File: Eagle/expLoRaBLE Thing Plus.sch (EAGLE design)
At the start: 65 parts, among them J2 CORTEX_DEBUG, J5 USB-C, J8 U.FL, U1 MCP73831, U2 3.3V, U3 NM180100, U4 CH340E_MSOP10, U6 DPX202700DT-4162A1, Y1 32.768kHz

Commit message: Create prelim board fabrication files
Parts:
- removed R10, R9: 10k, SparkFun-Resistors:10KOHM-0603-1/10W-1%
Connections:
- removed net LORA_EN: U3.GPIO7
- net 3.3V: no longer R10.2, R9.2
- net D14/QWIIC_SDA: no longer R10.1
- net ~D15/QWIIC_SCL: no longer R9.1
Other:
- moved on the sheet: TP4, TP5
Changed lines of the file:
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@@
 <part name="GND20" library="SparkFun-PowerSymbols" library_urn="urn:adsk.eagle:library:530" deviceset="GND" device=""/>
 <part name="J8" library="SparkFun-Connectors" library_urn="urn:adsk.eagle:library:513" deviceset="U.FL" device="" package3d_urn="urn:adsk.eagle:package:38237/1" override_package3d_urn="urn:adsk.eagle:package:23933012/2" override_package_urn="urn:adsk.eagle:footprint:37889/1" value="U.FL"/>
-<part name="R9" library="SparkFun-Resistors" library_urn="urn:adsk.eagle:library:23925323" deviceset="10KOHM" device="-0603-1/10W-1%" package3d_urn="urn:adsk.eagle:package:23925385/2" value="10k"/>
-<part name="R10" library="SparkFun-Resistors" library_urn="urn:adsk.eagle:library:23925323" deviceset="10KOHM" device="-0603-1/10W-1%" package3d_urn="urn:adsk.eagle:package:23925385/2" value="10k"/>
-<part name="SUPPLY21" library="SparkFun-PowerSymbols" library_urn="urn:adsk.eagle:library:530" deviceset="3.3V" device=""/>
-<part name="SUPPLY22" library="SparkFun-PowerSymbols" library_urn="urn:adsk.eagle:library:530" deviceset="3.3V" device=""/>
 </parts>
 <sheets>
@@
 </segment>
 </net>
-<net name="LORA_EN" class="0">
-<segment>
-<wire x1="63.5" y1="86.36" x2="60.96" y2="86.36" width="0.1524" layer="91"/>
-<label x="60.96" y="86.36" size="1.27" layer="95" font="vector" rot="R180" xref="yes"/>
-<pinref part="U3" gate="G$1" pin="GPIO7"/>
-</segment>
-</net>
 <net name="D10/SWCH" class="0">
 <segment>
@@
 <attribute name="VALUE" x="106.68" y="17.526" size="1.778" layer="96" font="vector" align="top-center"/>
 </instance>
-<instance part="TP4" gate="G$1" x="210.82" y="142.24" smashed="yes">
-<attribute name="NAME" x="214.63" y="141.478" size="1.778" layer="95" font="vector"/>
-</instance>
-<instance part="TP5" gate="G$1" x="210.82" y="134.62" smashed="yes">
-<attribute name="NAME" x="214.63" y="133.858" size="1.778" layer="95" font="vector"/>
+<instance part="TP4" gate="G$1" x="200.66" y="142.24" smashed="yes">
+<attribute name="NAME" x="204.47" y="141.478" size="1.778" layer="95" font="vector"/>
+</instance>
+<instance part="TP5" gate="G$1" x="200.66" y="134.62" smashed="yes">
+<attribute name="NAME" x="204.47" y="133.858" size="1.778" layer="95" font="vector"/>
 </instance>
 <instance part="U6" gate="A" x="172.72" y="68.58" smashed="yes">
@@
 <instance part="J8" gate="G$1" x="157.48" y="66.04" smashed="yes">
 <attribute name="NAME" x="153.67" y="70.104" size="1.778" layer="95"/>
-</instance>
-<instance part="R9" gate="G$1" x="193.04" y="149.86" smashed="yes" rot="R90">
-<attribute name="NAME" x="191.516" y="149.86" size="1.778" layer="95" font="vector" rot="R90" align="bottom-center"/>
-<attribute name="VALUE" x="194.564" y="149.86" size="1.778" layer="96" font="vector" rot="R90" align="top-center"/>
-</instance>
-<instance part="R10" gate="G$1" x="203.2" y="149.86" smashed="yes" rot="R90">
-<attribute name="NAME" x="201.676" y="149.86" size="1.778" layer="95" font="vector" rot="R90" align="bottom-center"/>
-<attribute name="VALUE" x="204.724" y="149.86" size="1.778" layer="96" font="vector" rot="R90" align="top-center"/>
-</instance>
-<instance part="SUPPLY21" gate="G$1" x="193.04" y="157.48" smashed="yes">
-<attribute name="VALUE" x="193.04" y="160.274" size="1.778" layer="96" align="bottom-center"/>
-</instance>
-<instance part="SUPPLY22" gate="G$1" x="203.2" y="157.48" smashed="yes">
-<attribute name="VALUE" x="203.2" y="160.274" size="1.778" layer="96" align="bottom-center"/>
 </instance>
 </instances>
@@
 <pinref part="SUPPLY12" gate="G$1" pin="3.3V"/>
 </segment>
-<segment>
-<pinref part="R9" gate="G$1" pin="2"/>
-<wire x1="193.04" y1="154.94" x2="193.04" y2="157.48" width="0.1524" layer="91"/>
-<pinref part="SUPPLY21" gate="G$1" pin="3.3V"/>
-</segment>
-<segment>
-<pinref part="R10" gate="G$1" pin="2"/>
-<wire x1="203.2" y1="154.94" x2="203.2" y2="157.48" width="0.1524" layer="91"/>
-<pinref part="SUPPLY22" gate="G$1" pin="3.3V"/>
-</segment>
 </net>
 <net name="D14/QWIIC_SDA" class="0">
 <segment>
 <pinref part="J6" gate="G$1" pin="3"/>
-<wire x1="185.42" y1="137.16" x2="203.2" y2="137.16" width="0.1524" layer="91"/>
-<label x="210.82" y="137.16" size="1.27" layer="95" font="vector" xref="yes"/>
+<wire x1="185.42" y1="137.16" x2="198.12" y2="137.16" width="0.1524" layer="91"/>
+<label x="200.66" y="137.16" size="1.27" layer="95" font="vector" xref="yes"/>
 <pinref part="TP5" gate="G$1" pin="1"/>
-<wire x1="203.2" y1="137.16" x2="208.28" y2="137.16" width="0.1524" layer="91"/>
-<wire x1="208.28" y1="137.16" x2="210.82" y2="137.16" width="0.1524" layer="91"/>
-<wire x1="210.82" y1="134.62" x2="208.28" y2="134.62" width="0.1524" layer="91"/>
-<wire x1="208.28" y1="134.62" x2="208.28" y2="137.16" width="0.1524" layer="91"/>
-<junction x="208.28" y="137.16"/>
-<pinref part="R10" gate="G$1" pin="1"/>
-<wire x1="203.2" y1="144.78" x2="203.2" y2="137.16" width="0.1524" layer="91"/>
-<junction x="203.2" y="137.16"/>
+<wire x1="198.12" y1="137.16" x2="200.66" y2="137.16" width="0.1524" layer="91"/>
+<wire x1="200.66" y1="134.62" x2="198.12" y2="134.62" width="0.1524" layer="91"/>
+<wire x1="198.12" y1="134.62" x2="198.12" y2="137.16" width="0.1524" layer="91"/>
+<junction x="198.12" y="137.16"/>
 </segment>
 </net>
@@
 <segment>
 <pinref part="J6" gate="G$1" pin="4"/>
-<wire x1="185.42" y1="139.7" x2="193.04" y2="139.7" width="0.1524" layer="91"/>
-<label x="210.82" y="139.7" size="1.27" layer="95" font="vector" xref="yes"/>
+<label x="200.66" y="139.7" size="1.27" layer="95" font="vector" xref="yes"/>
 <pinref part="TP4" gate="G$1" pin="1"/>
-<wire x1="193.04" y1="139.7" x2="208.28" y2="139.7" width="0.1524" layer="91"/>
-<wire x1="208.28" y1="139.7" x2="210.82" y2="139.7" width="0.1524" layer="91"/>
-<wire x1="210.82" y1="142.24" x2="208.28" y2="142.24" width="0.1524" layer="91"/>
-<wire x1="208.28" y1="142.24" x2="208.28" y2="139.7" width="0.1524" layer="91"/>
-<junction x="208.28" y="139.7"/>
-<pinref part="R9" gate="G$1" pin="1"/>
-<wire x1="193.04" y1="144.78" x2="193.04" y2="139.7" width="0.1524" layer="91"/>
-<junction x="193.04" y="139.7"/>
-</segment>
-</net>
+<wire x1="185.42" y1="139.7" x2="198.12" y2="139.7" width="0.1524" layer="91"/>
+<wire x1="198.12" y1="139.7" x2="200.66" y2="139.7" width="0.1524" layer="91"/>
+<wire x1="200.66" y1="142.24" x2="198.12" y2="142.24" width="0.1524" layer="91"/>
+<wire x1="198.12" y1="142.24" x2="198.12" y2="139.7" width="0.1524" layer="91"/>
+<junction x="198.12" y="139.7"/>
+</segment>
+</net>

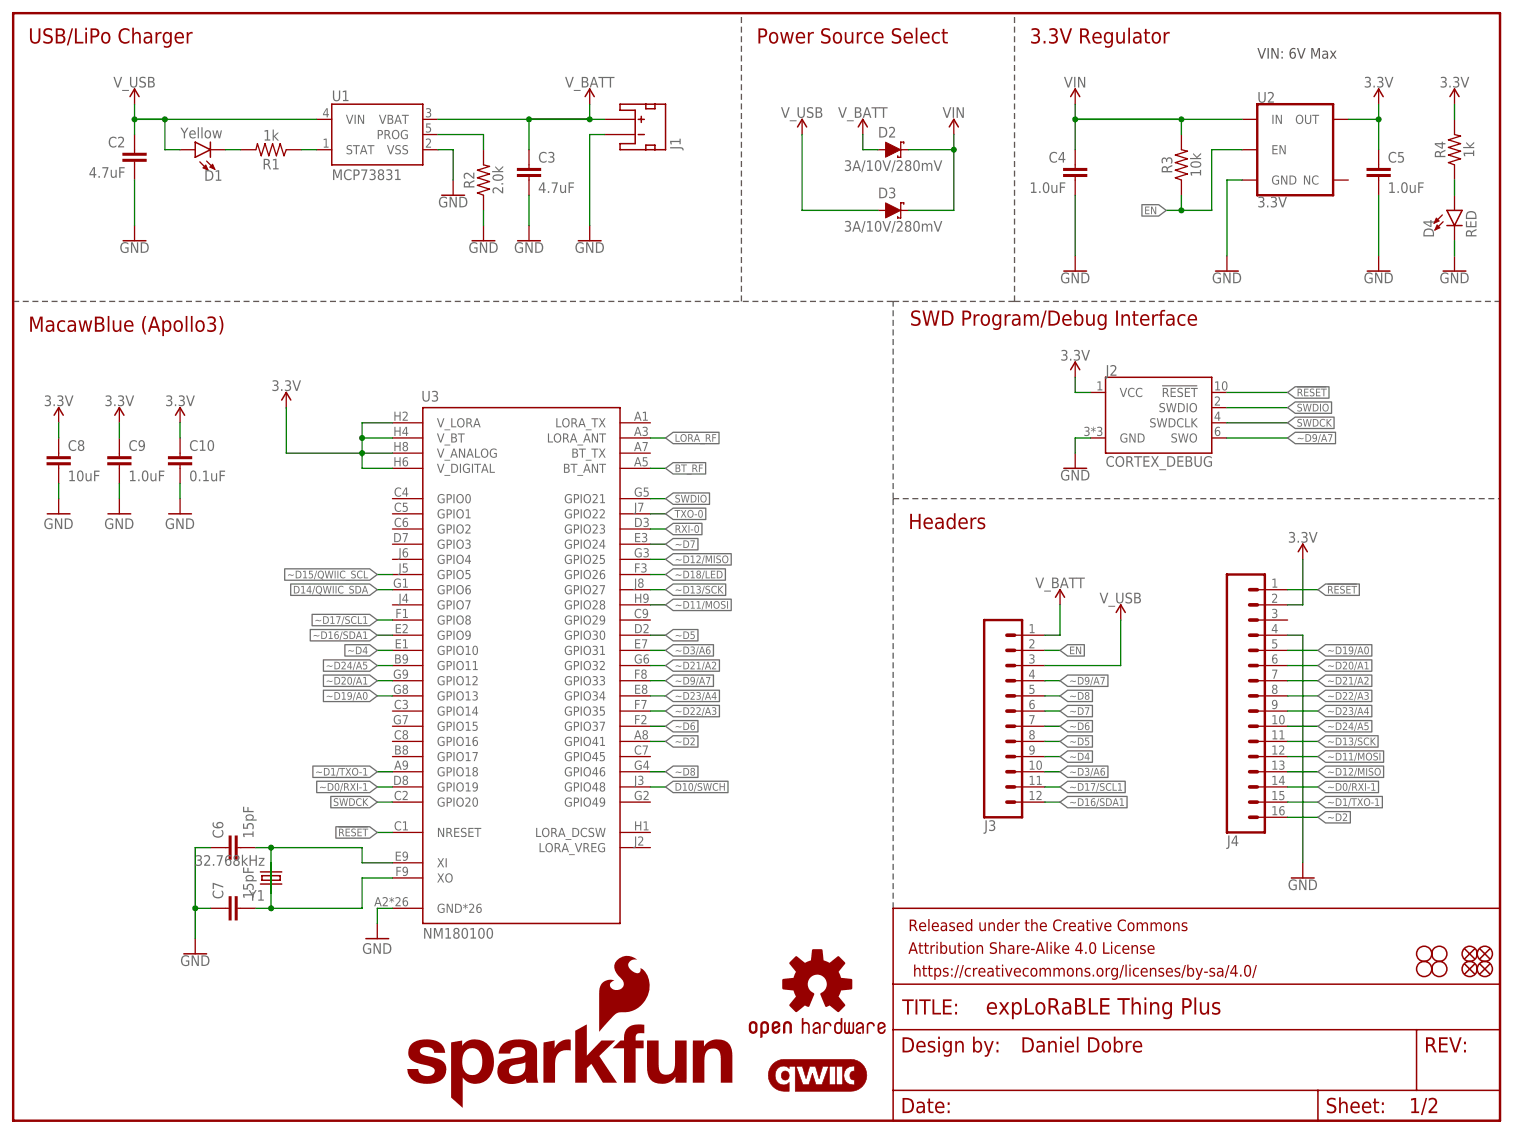
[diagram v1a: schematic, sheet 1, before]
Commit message: TP and Jumper addition
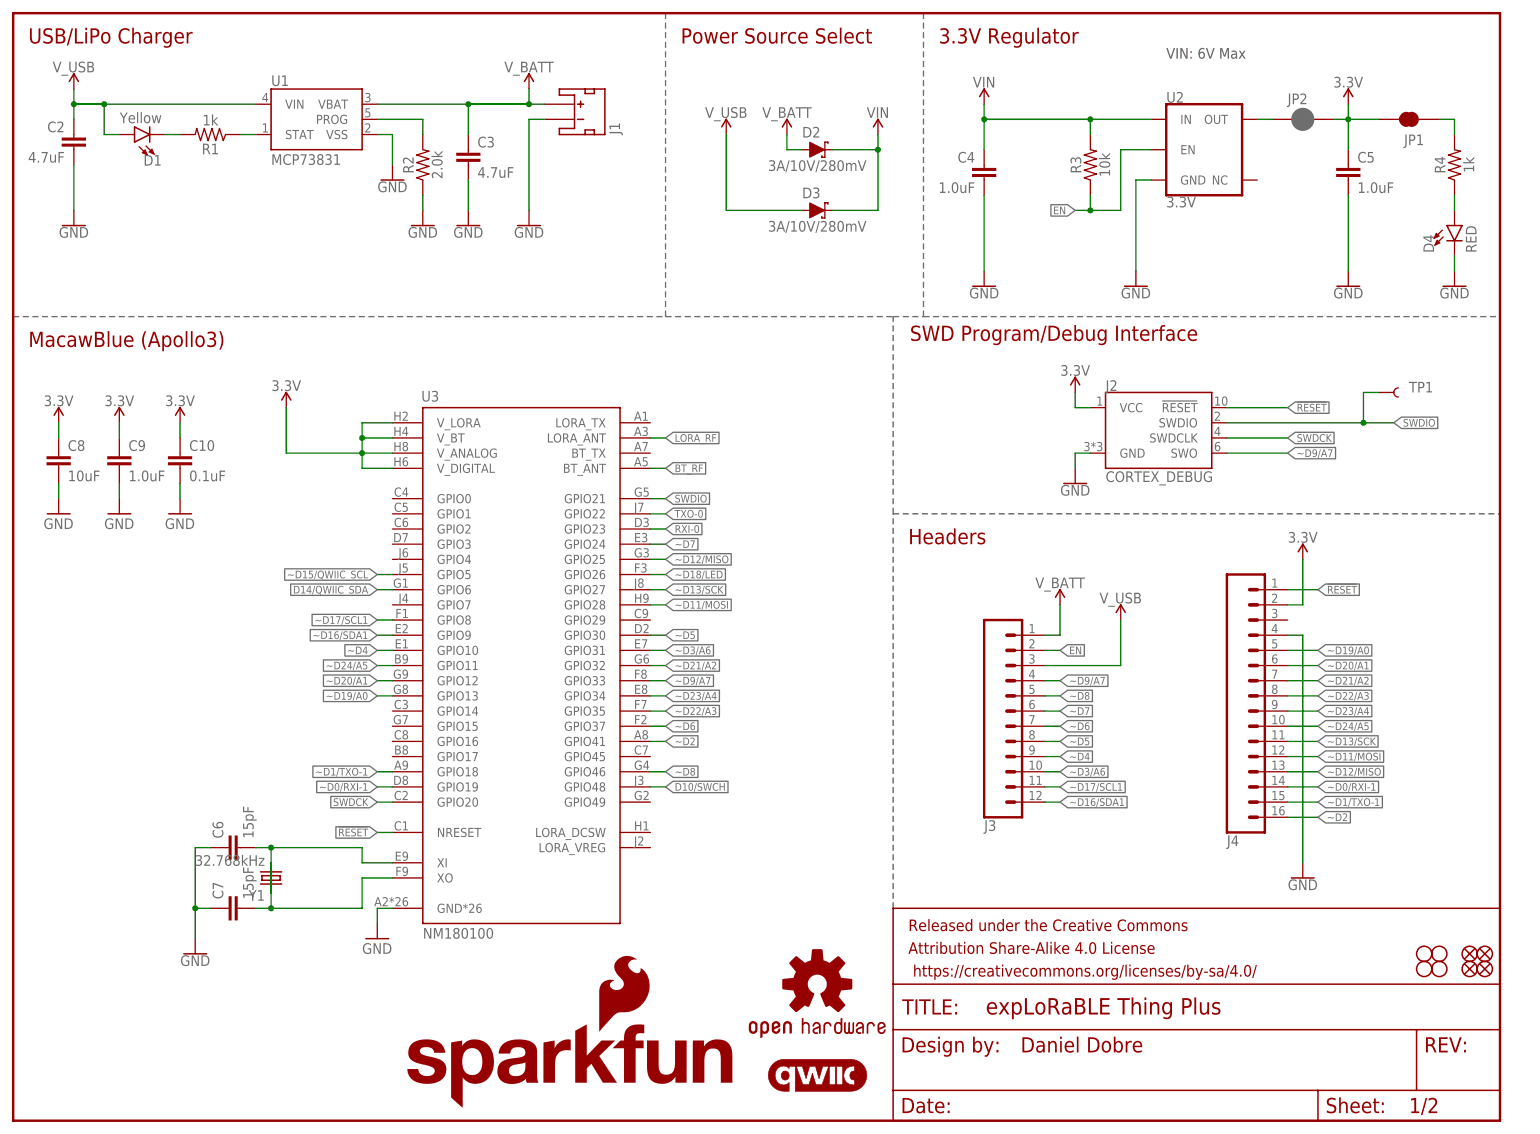
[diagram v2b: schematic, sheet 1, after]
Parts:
- added JP1: JUMPER-SMT_2_NC_TRACE_NO-SILK, SparkFun-Jumpers:JUMPER-SMT_2_NC_TRACE_NO-SILK
- added JP2: JUMPER-SMT_2_NC_PASTE_NO-SILK, SparkFun-Jumpers:JUMPER-SMT_2_NC_PASTE_NO-SILK
- added TP1: TEST-POINTTP_15TH_THRU, SparkFun-Connectors:TEST-POINTTP_15TH_THRU
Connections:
- new net N$14: JP2.1, U2.OUT
- new net N$6: JP1.1, R4.2
- net 3.3V: now also JP1.2, JP2.2; no longer R4.2, U2.OUT
- net SWDIO: now also TP1.1
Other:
- moved on the sheet: C2, C3, C4, C5, D1, D2, D3, D4, J1, J2, R1, R2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

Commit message: Updated labels to buzzard vectors and more minor tweaks
-also nudged some components near TX LED to make room for silk to avoid nearby mask.
-added version text object to both sch sheets
-redrew some sch to avoid 4-way nodes
-added buzzard label to bottom LED disable jumper
-moved ISO jumper to trace closed, added top silk label
-added special ordering instructions with 4-layer board text on tDocu
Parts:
- removed JP1: JUMPER-SMT_2_NC_TRACE_NO-SILK, SparkFun-Jumpers:JUMPER-SMT_2_NC_TRACE_NO-SILK
- removed JP2: JUMPER-SMT_2_NC_PASTE_NO-SILK, SparkFun-Jumpers:JUMPER-SMT_2_NC_PASTE_NO-SILK
- added ISO: JUMPER-SMT_2_NC_TRACE_NO-SILK, SparkFun-Jumpers:JUMPER-SMT_2_NC_TRACE_NO-SILK
- added LED: JUMPER-SMT_2_NC_TRACE_SILK, SparkFun-Jumpers:JUMPER-SMT_2_NC_TRACE_SILK
- added LOGO4: SPECIAL_INSTRUCTIONS-ORDERING, SparkFun-Aesthetics:SPECIAL_INSTRUCTIONS-ORDERING
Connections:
- net 3.3V: now also ISO.1, LED.2; no longer JP1.2, JP2.2
- net N$14: now also ISO.2; no longer JP2.1
- net N$6: now also LED.1; no longer JP1.1
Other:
- note added: "Cut ISO jumper to isolate 3.3V from upstream vreg"
- note added: "Cut LED jumper to disable power LED"
- note added: "v01"
- moved on the sheet: R3, TP2, TP3
